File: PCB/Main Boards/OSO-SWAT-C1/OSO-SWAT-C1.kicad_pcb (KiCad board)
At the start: 4 copper layers, 24.4 x 24.4 mm, 39 parts, among them J1 OSO_SWD, J2 FH19C-9S-0.5SH_10_, Q1 Q_Photo_NPN, U1 ATSAML22J18A-MUT, U2 MIC5365-3.3YC5-TR, X1 Crystal

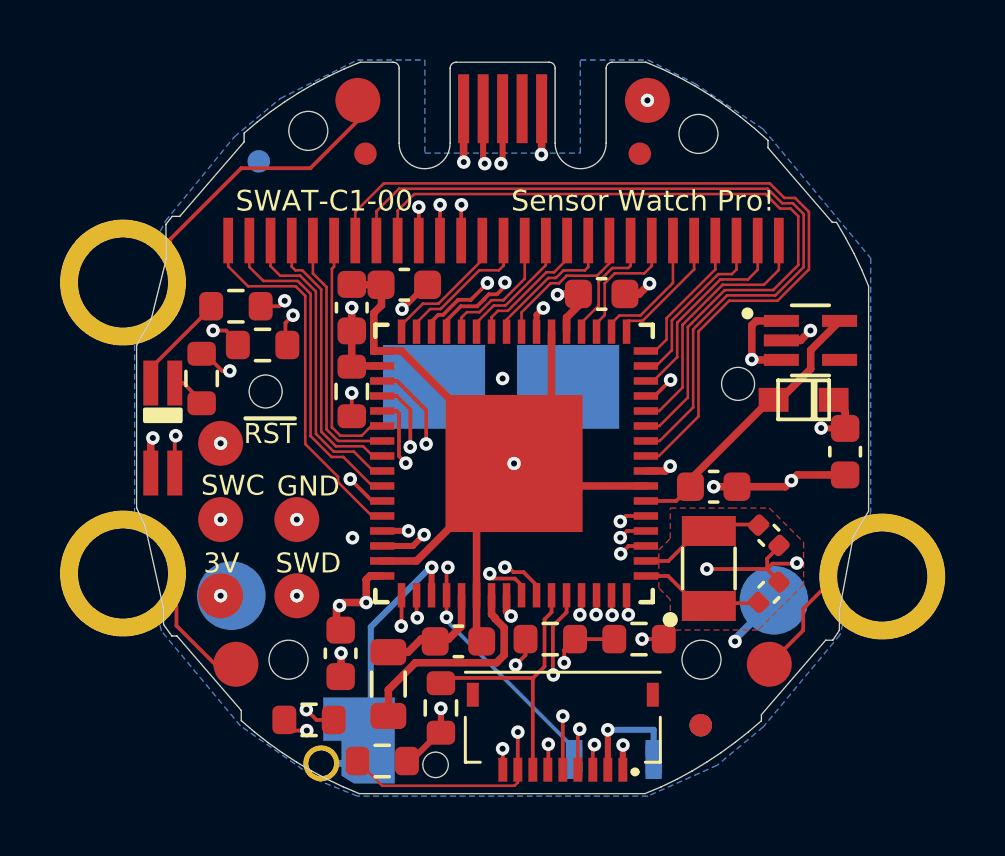
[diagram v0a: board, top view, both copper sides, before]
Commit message: WIP high voltage buzzer driver
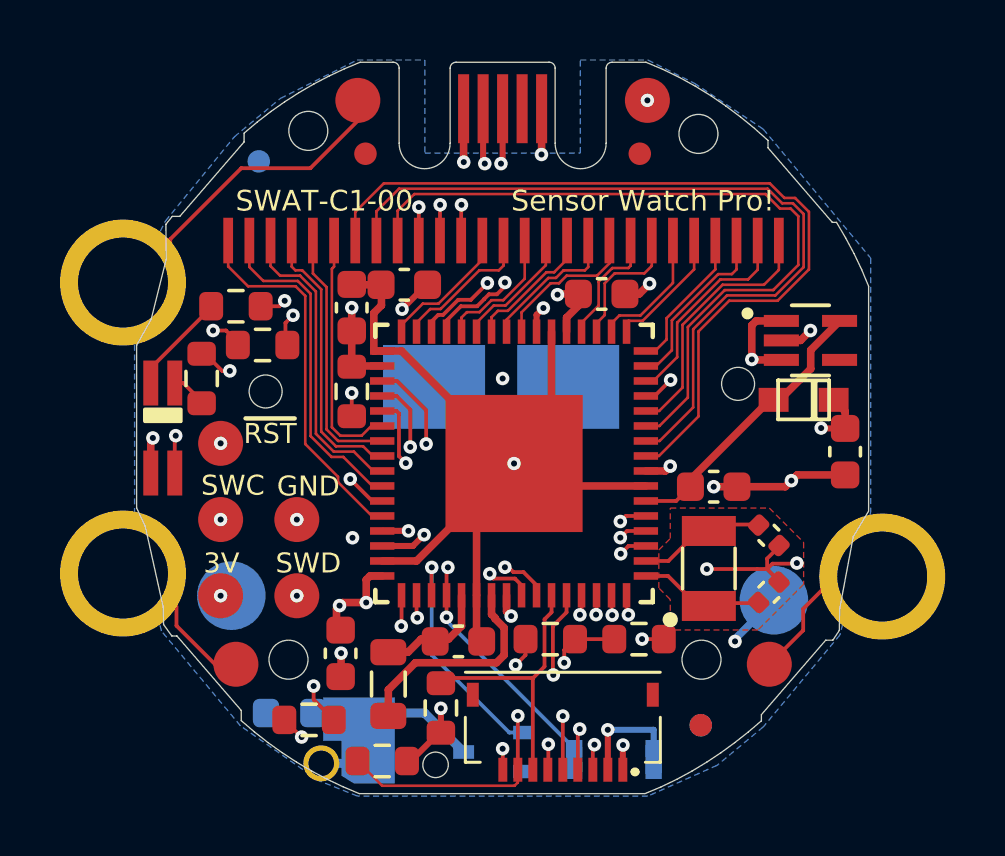
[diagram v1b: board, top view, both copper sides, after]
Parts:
- added L2: 10mH, Inductor_SMD:L_0603_1608Metric, B.Cu at (-7.10, 9.50)
- added Q2: Q_NMOS_GSD, Package_TO_SOT_SMD:SOT-323_SC-70, B.Cu at (-0.30, 10.8)
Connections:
- U$2 pad BUZZER: /BUZZER -> /BUZZER_HV
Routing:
- net /BUZZER_HV: track 0.00 -> 8.41 mm
- net /BUZZER: track 9.52 -> 7.99 mm
- net /LIGHTSENSE: track 25.8 -> 25.0 mm
